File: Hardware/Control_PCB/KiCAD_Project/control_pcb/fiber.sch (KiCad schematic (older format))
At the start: 10 parts, among them Q1 BSS138, U4 IF-D96F, U5 TC4S584F

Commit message: Draft of next layout
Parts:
- C17: renamed from C12; footprint Capacitors_SMD:C_0603_HandSoldering -> Capacitor_SMD:C_0603_1608Metric
- C18: renamed from C13; footprint Capacitors_SMD:C_0603_HandSoldering -> Capacitor_SMD:C_0603_1608Metric
- R37: renamed from R29; footprint Resistor_SMD:R_0603_1608Metric_Pad1.05x0.95mm_HandSolder -> Resistor_SMD:R_0603_1608Metric
- R38: renamed from R27; footprint Resistors_SMD:R_0603_HandSoldering -> Resistor_SMD:R_0603_1608Metric
- R39: renamed from R28; footprint Resistors_SMD:R_0603_HandSoldering -> Resistor_SMD:R_0603_1608Metric
- R40: renamed from R18; value NP -> 0R0; footprint Resistors_SMD:R_0603_HandSoldering -> Resistor_SMD:R_0603_1608Metric; Internal Part Number 0-0000000 -> 1-0000006; Populated 0 -> 1
- R41: renamed from R19; value 0R0 -> NP; footprint Resistors_SMD:R_0603_HandSoldering -> Resistor_SMD:R_0603_1608Metric; Populated 1 -> 0
- renumbered U4 to U5, U5 to U6
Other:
- note added: "Receives the fiber optic signal, buffers, and creates a level shifted serial output of the\nsignal. Optionally can invert the signal if the transmitter is ever changed."
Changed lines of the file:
@@
 $EndDescr
 $Comp
-L lib_sch:TC4S584F U5
+L lib_sch:TC4S584F U6
 U 1 1 5DEFBA5E
 P 5725 3750
-F 0 "U5" H 6069 3796 50  0000 L CNN
+F 0 "U6" H 6069 3796 50  0000 L CNN
 F 1 "TC4S584F" H 6069 3705 50  0000 L CNN
 F 2 "lib_fp:SOT753" H 5725 3750 50  0001 C CNN
@@
 $EndComp
 $Comp
-L lib_sch:IF-D96F U4
+L lib_sch:IF-D96F U5
 U 1 1 5DEFC09E
 P 4550 3750
-F 0 "U4" H 4197 3796 50  0000 R CNN
+F 0 "U5" H 4197 3796 50  0000 R CNN
 F 1 "IF-D96F" H 4197 3705 50  0000 R CNN
 F 2 "lib_fp:IF-D96F" H 4150 3750 50  0001 C CNN
@@
 $EndComp
 $Comp
-L power:+BATT #PWR028
+L power:+BATT #PWR049
 U 1 1 5DEFC7EC
 P 4550 3125
-F 0 "#PWR028" H 4550 2975 50  0001 C CNN
+F 0 "#PWR049" H 4550 2975 50  0001 C CNN
 F 1 "+BATT" H 4565 3298 50  0000 C CNN
 F 2 "" H 4550 3125 50  0001 C CNN
@@
 P 4350 3225
 AR Path="/5DED0CD0/5DEFD0D7" Ref="C?"  Part="1"
-AR Path="/5DEF9AB5/5DEFD0D7" Ref="C12"  Part="1"
-F 0 "C12" V 4225 3050 50  0000 C CNN
+AR Path="/5DEF9AB5/5DEFD0D7" Ref="C17"  Part="1"
+F 0 "C17" V 4225 3050 50  0000 C CNN
 F 1 "0.1u" V 4300 3100 50  0000 C CNN
-F 2 "Capacitors_SMD:C_0603_HandSoldering" H 4388 3075 50  0001 C CNN
+F 2 "Capacitor_SMD:C_0603_1608Metric" H 4388 3075 50  0001 C CNN
 F 3 "~" H 4350 3225 50  0001 C CNN
 F 4 "1-0000007" H 4350 3225 50  0001 C CNN "Internal Part Number"
@@
 P 5525 3225
 AR Path="/5DED0CD0/5DEFD4FE" Ref="C?"  Part="1"
-AR Path="/5DEF9AB5/5DEFD4FE" Ref="C13"  Part="1"
-F 0 "C13" V 5400 3050 50  0000 C CNN
+AR Path="/5DEF9AB5/5DEFD4FE" Ref="C18"  Part="1"
+F 0 "C18" V 5400 3050 50  0000 C CNN
 F 1 "0.1u" V 5475 3100 50  0000 C CNN
-F 2 "Capacitors_SMD:C_0603_HandSoldering" H 5563 3075 50  0001 C CNN
+F 2 "Capacitor_SMD:C_0603_1608Metric" H 5563 3075 50  0001 C CNN
 F 3 "~" H 5525 3225 50  0001 C CNN
 F 4 "1-0000007" H 5525 3225 50  0001 C CNN "Internal Part Number"
@@
 $EndComp
 $Comp
-L power:GND #PWR027
+L power:GND #PWR051
 U 1 1 5DEFDC89
 P 4200 3225
-F 0 "#PWR027" H 4200 2975 50  0001 C CNN
+F 0 "#PWR051" H 4200 2975 50  0001 C CNN
 F 1 "GND" H 4205 3052 50  0000 C CNN
 F 2 "" H 4200 3225 50  0001 C CNN
@@
 $EndComp
 $Comp
-L power:GND #PWR030
+L power:GND #PWR052
 U 1 1 5DEFE20B
 P 5375 3225
-F 0 "#PWR030" H 5375 2975 50  0001 C CNN
+F 0 "#PWR052" H 5375 2975 50  0001 C CNN
 F 1 "GND" H 5380 3052 50  0000 C CNN
 F 2 "" H 5375 3225 50  0001 C CNN
@@
 	4550 3225 4550 3450
 $Comp
-L power:+BATT #PWR031
+L power:+BATT #PWR050
 U 1 1 5DEFE7FA
 P 5725 3125
-F 0 "#PWR031" H 5725 2975 50  0001 C CNN
+F 0 "#PWR050" H 5725 2975 50  0001 C CNN
 F 1 "+BATT" H 5740 3298 50  0000 C CNN
 F 2 "" H 5725 3125 50  0001 C CNN
@@
 	5725 3225 5725 3450
 $Comp
-L power:GND #PWR029
+L power:GND #PWR055
 U 1 1 5DEFF1D2
 P 4550 4050
-F 0 "#PWR029" H 4550 3800 50  0001 C CNN
+F 0 "#PWR055" H 4550 3800 50  0001 C CNN
 F 1 "GND" H 4555 3877 50  0000 C CNN
 F 2 "" H 4550 4050 50  0001 C CNN
@@
 $EndComp
 $Comp
-L power:GND #PWR032
+L power:GND #PWR056
 U 1 1 5DEFF4CF
 P 5725 4050
-F 0 "#PWR032" H 5725 3800 50  0001 C CNN
+F 0 "#PWR056" H 5725 3800 50  0001 C CNN
 F 1 "GND" H 5730 3877 50  0000 C CNN
 F 2 "" H 5725 4050 50  0001 C CNN
@@
 	5350 3750 5425 3750
 $Comp
-L Device:R R19
+L Device:R R41
 U 1 1 5DEFFB46
 P 6475 4375
-F 0 "R19" V 6425 4175 50  0000 C CNN
-F 1 "0R0" V 6475 4375 50  0000 C CNN
-F 2 "Resistors_SMD:R_0603_HandSoldering" V 6405 4375 50  0001 C CNN
+F 0 "R41" V 6425 4175 50  0000 C CNN
+F 1 "NP" V 6475 4375 50  0000 C CNN
+F 2 "Resistor_SMD:R_0603_1608Metric" V 6405 4375 50  0001 C CNN
 F 3 "~" H 6475 4375 50  0001 C CNN
 F 4 "1-0000006" H 6475 4375 50  0001 C CNN "Internal Part Number"
-F 5 "1" H 6475 4375 50  0001 C CNN "Populated"
+F 5 "0" H 6475 4375 50  0001 C CNN "Populated"
 	1    6475 4375
 	0    1    1    0
 $EndComp
 $Comp
-L Device:R R18
+L Device:R R40
 U 1 1 5DF001E3
 P 6475 4225
-F 0 "R18" V 6425 4025 50  0000 C CNN
-F 1 "NP" V 6475 4225 50  0000 C CNN
-F 2 "Resistors_SMD:R_0603_HandSoldering" V 6405 4225 50  0001 C CNN
+F 0 "R40" V 6425 4025 50  0000 C CNN
+F 1 "0R0" V 6475 4225 50  0000 C CNN
+F 2 "Resistor_SMD:R_0603_1608Metric" V 6405 4225 50  0001 C CNN
 F 3 "~" H 6475 4225 50  0001 C CNN
-F 4 "0-0000000" H 6475 4225 50  0001 C CNN "Internal Part Number"
-F 5 "0" H 6475 4225 50  0001 C CNN "Populated"
+F 4 "1-0000006" H 6475 4225 50  0001 C CNN "Internal Part Number"
+F 5 "1" H 6475 4225 50  0001 C CNN "Populated"
 	1    6475 4225
 	0    1    1    0
@@
 P 6750 4100
 AR Path="/5DEB1E7E" Ref="R?"  Part="1"
-AR Path="/5DEF9AB5/5DEB1E7E" Ref="R27"  Part="1"
-F 0 "R27" V 6825 4050 50  0000 L CNN
+AR Path="/5DEF9AB5/5DEB1E7E" Ref="R38"  Part="1"
+F 0 "R38" V 6825 4050 50  0000 L CNN
 F 1 "10k" V 6750 4025 50  0000 L CNN
-F 2 "Resistors_SMD:R_0603_HandSoldering" V 6680 4100 50  0001 C CNN
+F 2 "Resistor_SMD:R_0603_1608Metric" V 6680 4100 50  0001 C CNN
 F 3 "~" H 6750 4100 50  0001 C CNN
 F 4 "1-0000010" H 6750 4100 50  0001 C CNN "Internal Part Number"
@@
 	6750 4300 6825 4300
 $Comp
-L power:+BATT #PWR0112
+L power:+BATT #PWR053
 U 1 1 5DEB629F
 P 6750 3850
-F 0 "#PWR0112" H 6750 3700 50  0001 C CNN
+F 0 "#PWR053" H 6750 3700 50  0001 C CNN
 F 1 "+BATT" H 6765 4023 50  0000 C CNN
 F 2 "" H 6750 3850 50  0001 C CNN
@@
 P 7300 4100
 AR Path="/5DEB711A" Ref="R?"  Part="1"
-AR Path="/5DEF9AB5/5DEB711A" Ref="R28"  Part="1"
-F 0 "R28" V 7375 4050 50  0000 L CNN
+AR Path="/5DEF9AB5/5DEB711A" Ref="R39"  Part="1"
+F 0 "R39" V 7375 4050 50  0000 L CNN
 F 1 "10k" V 7300 4025 50  0000 L CNN
-F 2 "Resistors_SMD:R_0603_HandSoldering" V 7230 4100 50  0001 C CNN
+F 2 "Resistor_SMD:R_0603_1608Metric" V 7230 4100 50  0001 C CNN
 F 3 "~" H 7300 4100 50  0001 C CNN
 F 4 "1-0000010" H 7300 4100 50  0001 C CNN "Internal Part Number"
@@
 	7300 3900 7300 3950
 $Comp
-L power:+3V3 #PWR0113
+L power:+3V3 #PWR054
 U 1 1 5DEB82C0
 P 7300 3850
-F 0 "#PWR0113" H 7300 3700 50  0001 C CNN
+F 0 "#PWR054" H 7300 3700 50  0001 C CNN
 F 1 "+3V3" H 7315 4023 50  0000 C CNN
 F 2 "" H 7300 3850 50  0001 C CNN
@@
 Connection ~ 7300 4300
 $Comp
-L Device:R R29
+L Device:R R37
 U 1 1 5E83CB68
 P 4975 3500
-F 0 "R29" V 5050 3450 50  0000 L CNN
+F 0 "R37" V 5050 3450 50  0000 L CNN
 F 1 "10k" V 4975 3425 50  0000 L CNN
-F 2 "Resistor_SMD:R_0603_1608Metric_Pad1.05x0.95mm_HandSolder" V 4905 3500 50  0001 C CNN
+F 2 "Resistor_SMD:R_0603_1608Metric" V 4905 3500 50  0001 C CNN
 F 3 "~" H 4975 3500 50  0001 C CNN
 F 4 "1-0000010" H 4975 3500 50  0001 C CNN "Internal Part Number"
@@
 Wire Wire Line
 	4975 3225 4550 3225
+Text Notes 7600 750  0    50   ~ 0
+Receives the fiber optic signal, buffers, and creates a level shifted serial output of the\nsignal. Optionally can invert the signal if the transmitter is ever changed.
 $EndSCHEMATC

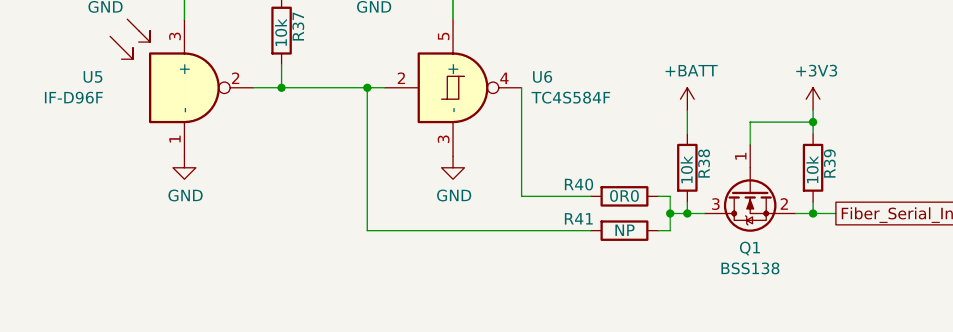
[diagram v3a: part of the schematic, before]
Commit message: Add PNP files and minor schematic bumps
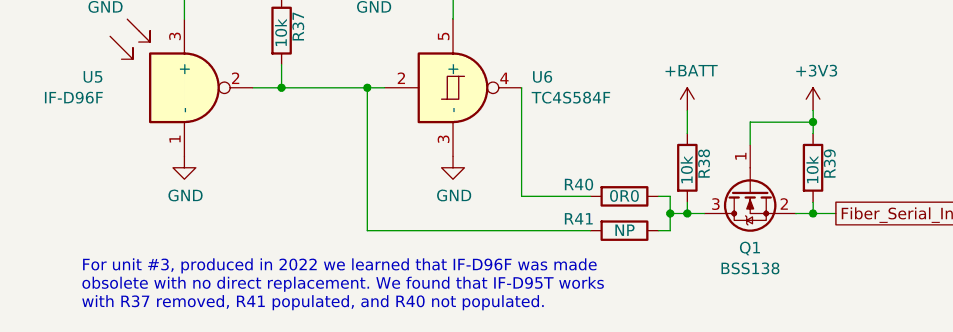
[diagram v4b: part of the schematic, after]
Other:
- note added: "For unit #3, produced in 2022 we learned that IF-D96F was made\nobsolete with no direct replacement. We found that IF-D95T works\nwith R37 removed, R41 populated, and R40 not populated."
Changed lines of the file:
@@
 Text Notes 7600 750  0    50   ~ 0
 Receives the fiber optic signal, buffers, and creates a level shifted serial output of the\nsignal. Optionally can invert the signal if the transmitter is ever changed.
+Text Notes 4100 4725 0    50   ~ 0
+For unit #3, produced in 2022 we learned that IF-D96F was made\nobsolete with no direct replacement. We found that IF-D95T works\nwith R37 removed, R41 populated, and R40 not populated.
 $EndSCHEMATC
